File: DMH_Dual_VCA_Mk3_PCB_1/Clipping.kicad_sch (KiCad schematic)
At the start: 7 parts, among them SW3 SW_DPDT_x2

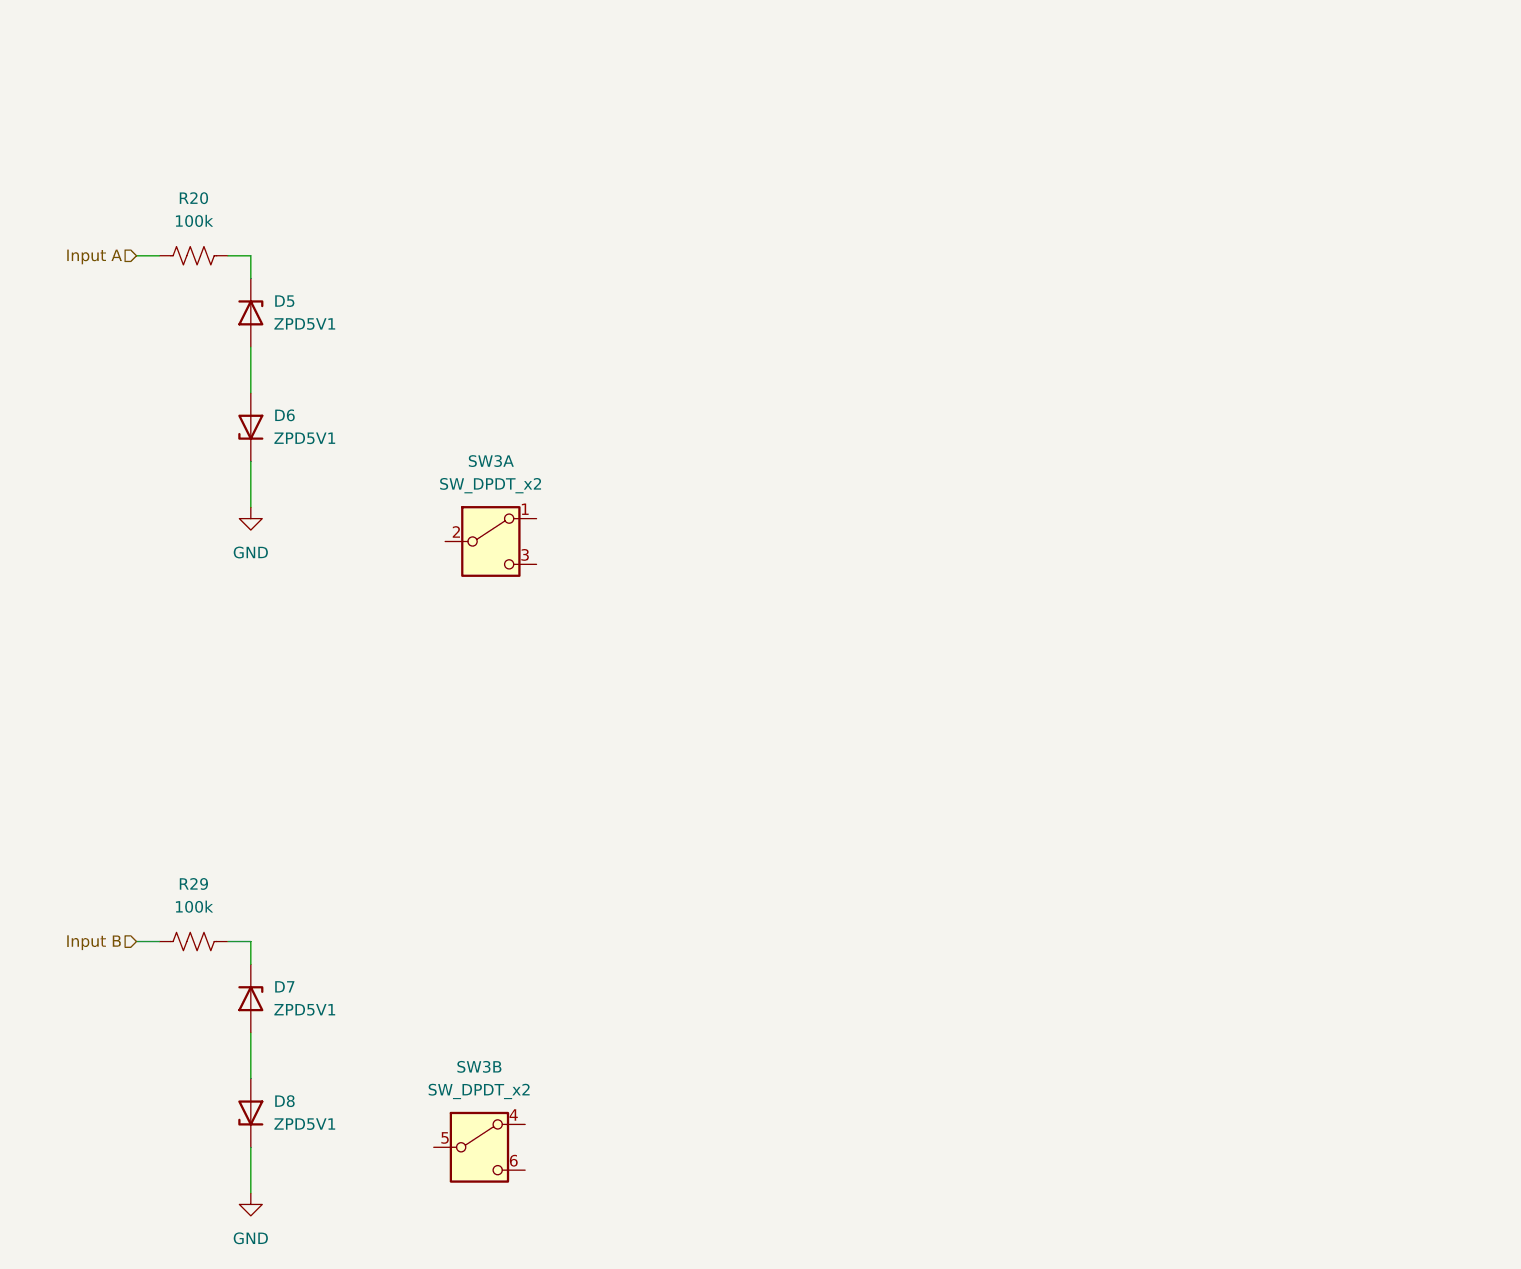
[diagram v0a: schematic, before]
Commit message: Designed clip and dist circuit
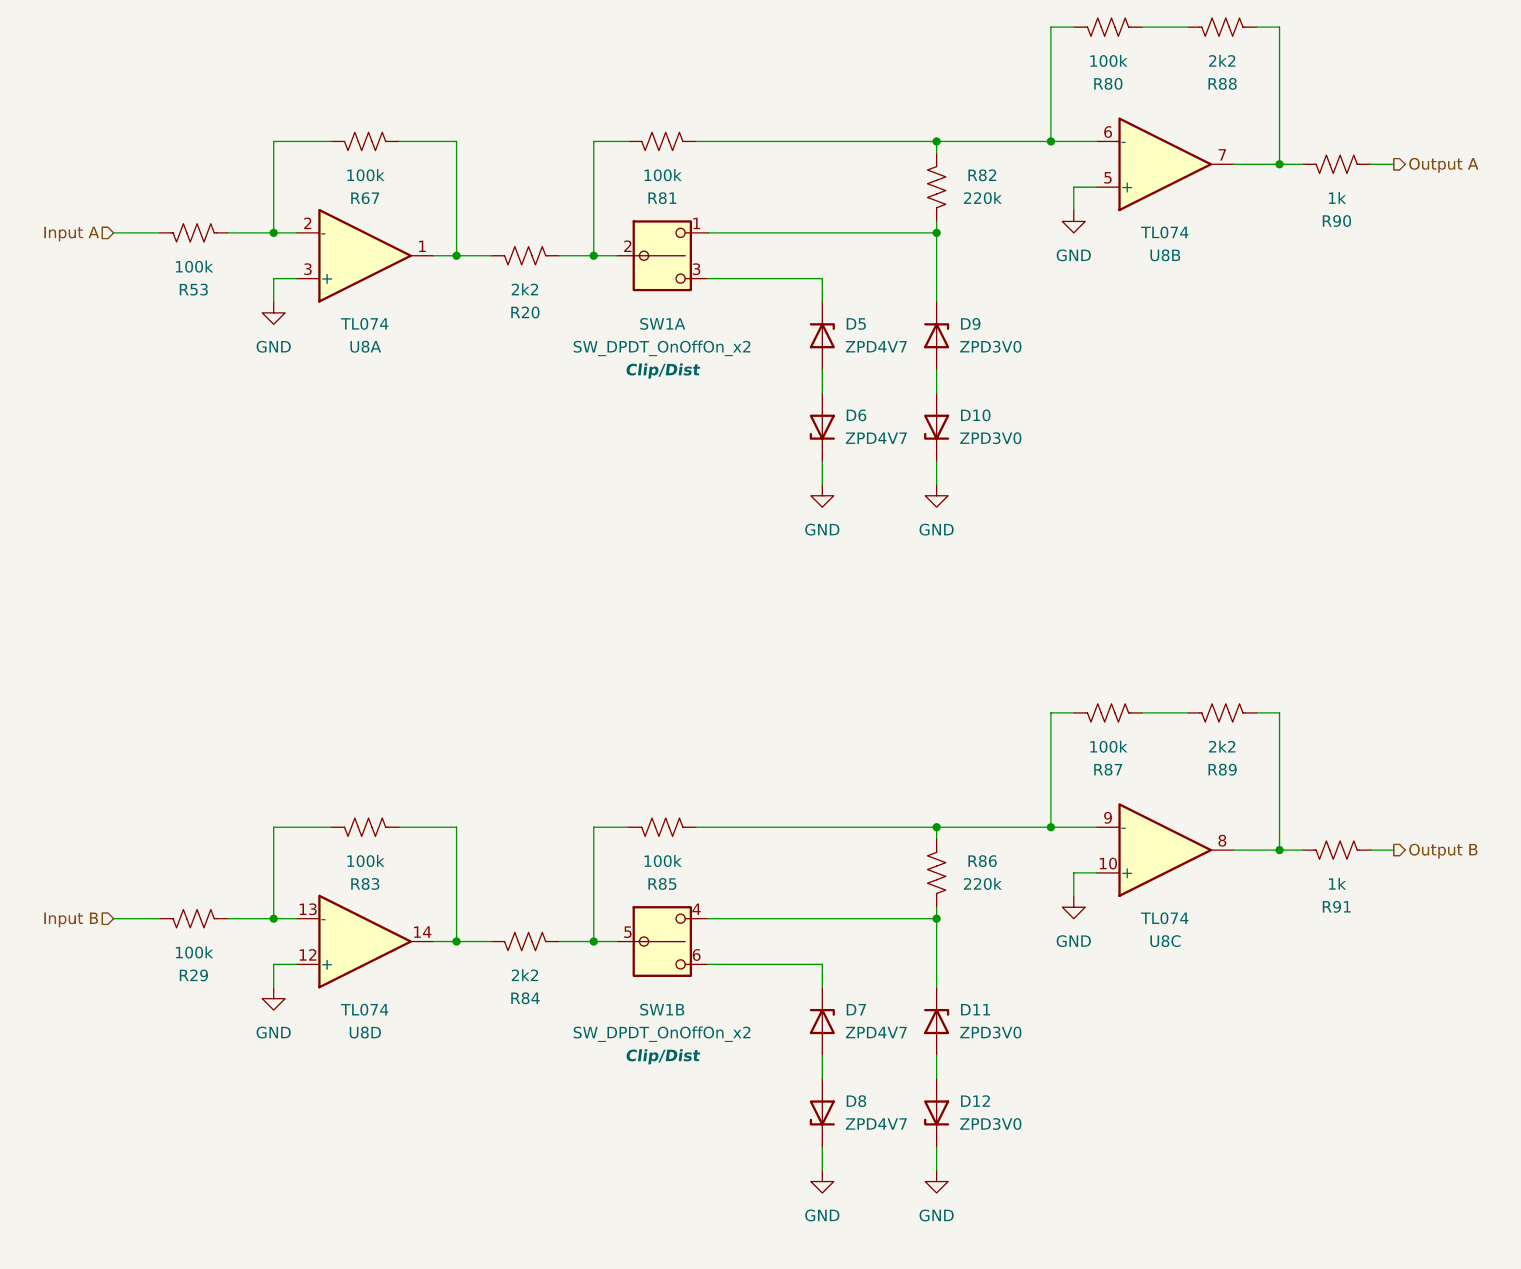
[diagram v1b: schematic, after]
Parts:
- removed SW3: SW_DPDT_x2, symbol Switch:SW_DPDT_x2
- added D10, D11, D12, D9: ZPD3V0, Diode_THT:D_DO-35_SOD27_P7.62mm_Horizontal, symbol Diode:ZPDxx
- added R53, R67, R80, R81, R83, R85, R87: 100k, Resistor_THT:R_Axial_DIN0207_L6.3mm_D2.5mm_P7.62mm_Horizontal, symbol Device:R_US
- added R82, R86: 220k, Resistor_THT:R_Axial_DIN0207_L6.3mm_D2.5mm_P7.62mm_Horizontal, symbol Device:R_US
- added R84, R88, R89: 2k2, Resistor_THT:R_Axial_DIN0207_L6.3mm_D2.5mm_P7.62mm_Horizontal, symbol Device:R_US
- added R90, R91: 1k, Resistor_THT:R_Axial_DIN0207_L6.3mm_D2.5mm_P7.62mm_Horizontal, symbol Device:R_US
- added SW1: SW_DPDT_OnOffOn_x2, SynthStuff:Toggle_Switch_2_Poles_TE, symbol SynthStuff:SW_DPDT_OnOffOn_x2
- added U8: TL074, Package_DIP:DIP-14_W7.62mm_Socket, symbol Amplifier_Operational:TL074
- D5, D6, D7, D8: value ZPD5V1 -> ZPD4V7
- R20: value 100k -> 2k2
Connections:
- net GND: now also D10.1 (K), D12.1 (K), U8.10 (+), U8.12 (+), U8.3 (+), U8.5 (+)
- net Input A: now also R53.1; no longer R20.1
- net at D7.1 (K): now also SW1.6 (C); no longer R29.2
- net at D5.1 (K): now also SW1.3 (C); no longer R20.2
- new net: D9.1 (K), R82.1, SW1.1 (A)
- new net: R80.1, R81.2, R82.2, U8.6 (-)
- new net: R89.2, R91.1, U8.8
- new net: R85.2, R86.2, R87.1, U8.9 (-)
- new net: D11.2 (A), D12.2 (A)
- new net: R80.2, R88.1
- new net: R88.2, R90.1, U8.7
- new net: D11.1 (K), R86.1, SW1.4 (A)
- new net: R84.2, R85.1, SW1.5 (B)
- new net: R87.2, R89.1
- new net: R83.1, R84.1, U8.14
- new net: R20.1, R67.1, U8.1
- new net: R53.2, R67.2, U8.2 (-)
- new net: D10.2 (A), D9.2 (A)
- new net: R29.2, R83.2, U8.13 (-)
- new net: R20.2, R81.1, SW1.2 (B)
- new net Output A: R90.2
- new net Output B: R91.2
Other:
- moved on the sheet: D5, D6, R20
